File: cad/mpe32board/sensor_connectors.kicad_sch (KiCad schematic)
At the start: 41 parts, among them J10 Conn_01x06, J11 Conn_01x06, J12 Conn_01x06, J13 Conn_01x06, J14 Conn_01x06, J15 Conn_01x06, J16 Conn_01x06, J17 Conn_01x06, J18 Conn_01x06, J19 Conn_01x06, J20 Conn_01x06, J21 Conn_01x06, J22 Conn_01x06, J23 Conn_01x06, J24 Conn_01x06, J25 Conn_01x06, J26 Conn_01x06, J27 Conn_01x06, J28 Conn_01x06, J29 Conn_01x06, J3 Conn_01x04, J30 Conn_01x06, J31 Conn_01x06, J32 Conn_01x06, J33 Conn_01x06, J34 Conn_01x06, J35 Conn_01x06, J36 Conn_01x06, J37 Conn_01x06, J38 Conn_01x06, J39 Conn_01x06, J4 Conn_01x06, J40 Conn_01x06, J41 Conn_01x06, J42 Conn_01x06, J43 Conn_01x06, J5 Conn_01x06, J6 Conn_01x06, J7 Conn_01x06, J8 Conn_01x06, J9 Conn_01x06

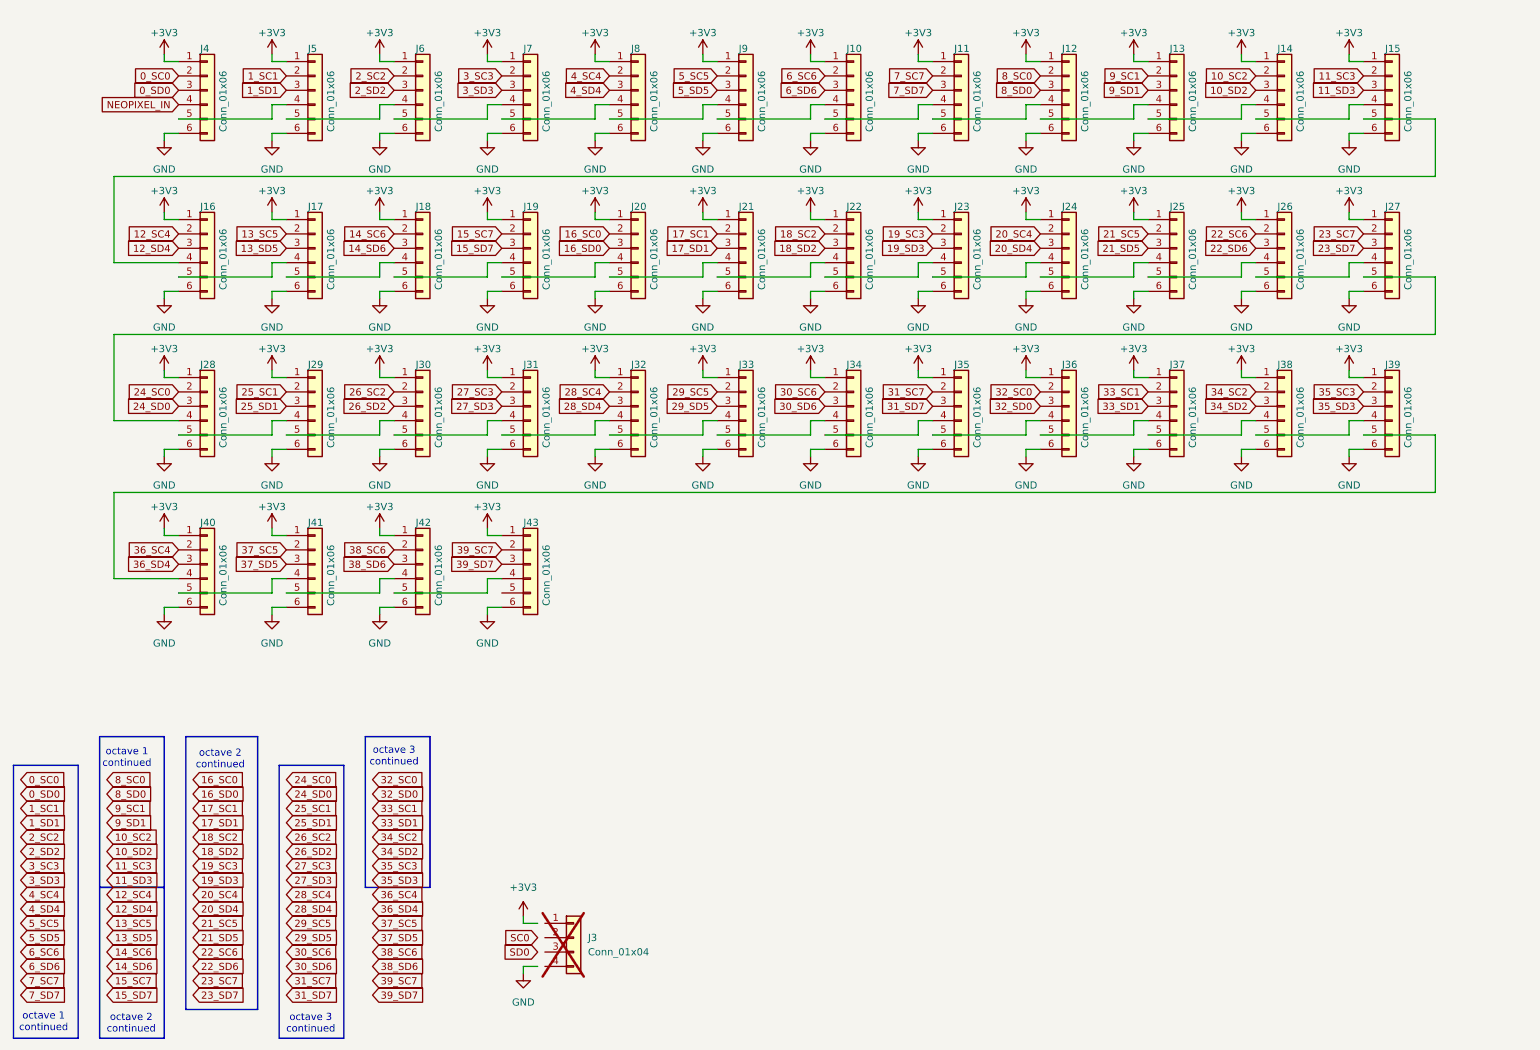
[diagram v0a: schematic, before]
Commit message: add sdram
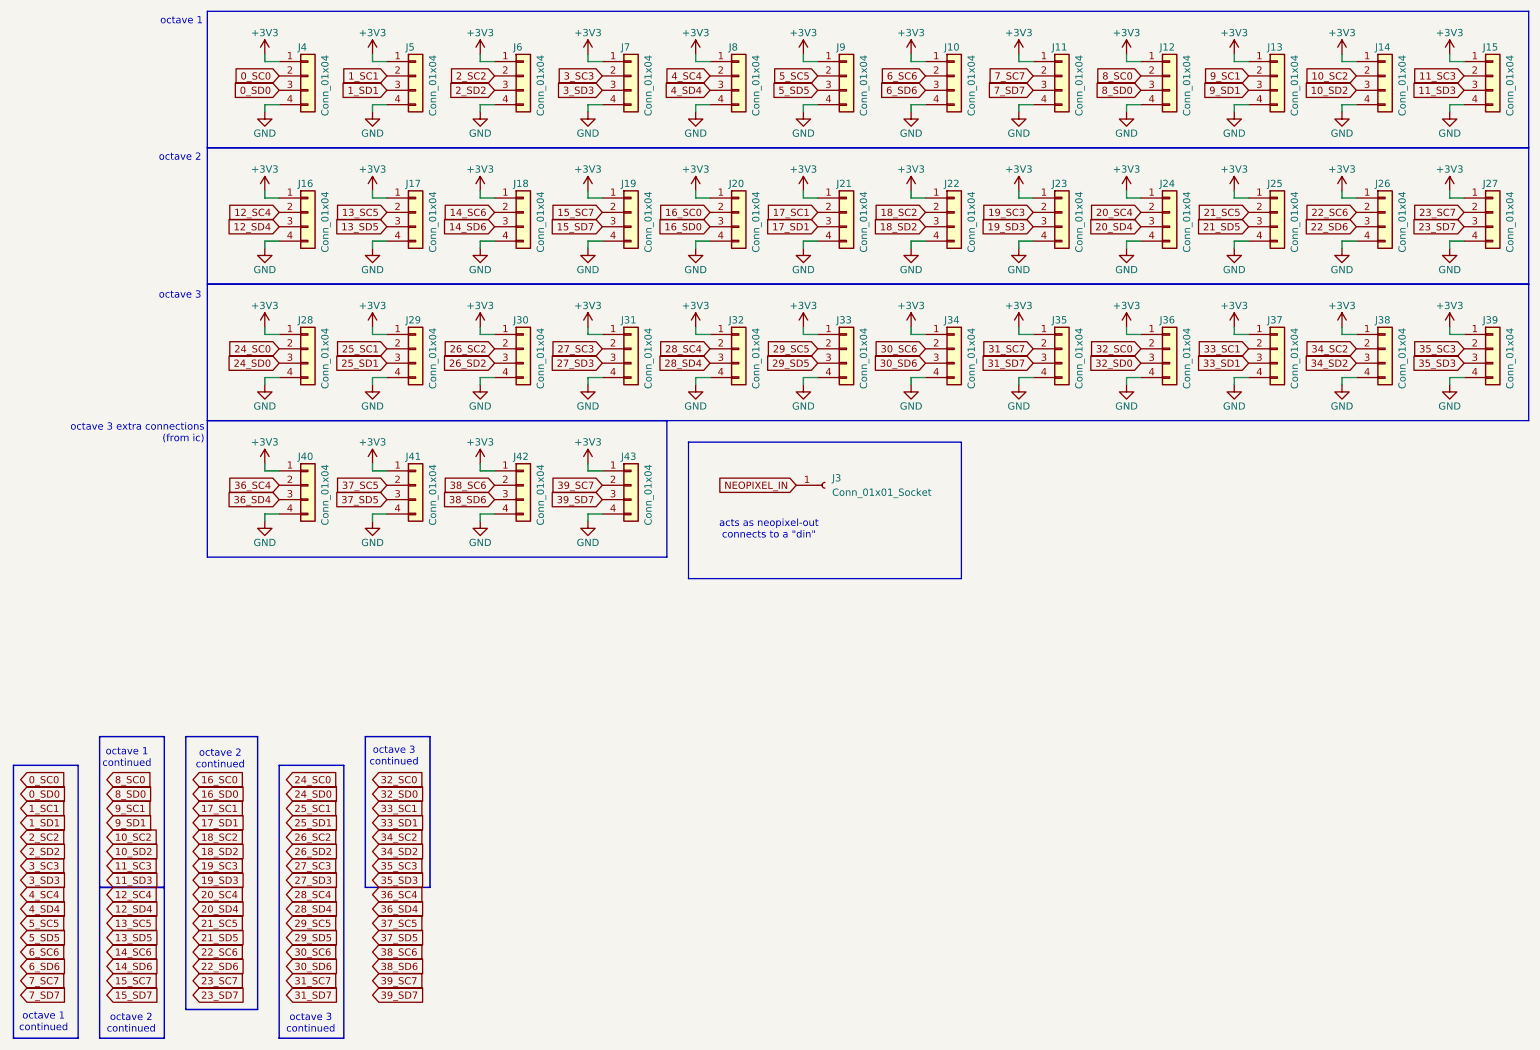
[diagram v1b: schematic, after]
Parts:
- removed J10, J11, J12, J13, J14, J15, J16, J17, J18, J19, J20, J21, J22, J23, J24, J25, J26, J27, J28, J29, J30, J31, J32, J33, J34, J35, J36, J37, J38, J39, J4, J40, J41, J42, J43, J5, J6, J7, J8, J9: Conn_01x06, Connector_JST:JST_SH_BM06B-SRSS-TB_1x06-1MP_P1.00mm_Vertical, symbol Connector_Generic:Conn_01x06
- removed J3: Conn_01x04, Connector_JST:JST_SH_BM04B-SRSS-TB_1x04-1MP_P1.00mm_Vertical, symbol Connector_Generic:Conn_01x04
- added J10, J11, J12, J13, J14, J15, J16, J17, J18, J19, J20, J21, J22, J23, J24, J25, J26, J27, J28, J29, J30, J31, J32, J33, J34, J35, J36, J37, J38, J39, J40, J41, J42, J43, J5, J6, J7, J8, J9: Conn_01x04, symbol Connector_Generic:Conn_01x04
- added J3: Conn_01x01_Socket, Connector_PinSocket_2.54mm:PinSocket_1x01_P2.54mm_Vertical, symbol Connector:Conn_01x01_Socket
- added J4: Conn_01x04, Connector_JST:JST_SH_BM04B-SRSS-TB_1x04-1MP_P1.00mm_Vertical, symbol Connector_Generic:Conn_01x04
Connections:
- net +3V3: now also J10.1 (Pin_1), J11.1 (Pin_1), J12.1 (Pin_1), J13.1 (Pin_1), J14.1 (Pin_1), J15.1 (Pin_1), J16.1 (Pin_1), J17.1 (Pin_1), J18.1 (Pin_1), J19.1 (Pin_1), J20.1 (Pin_1), J21.1 (Pin_1), J22.1 (Pin_1), J23.1 (Pin_1), J24.1 (Pin_1), J25.1 (Pin_1), J26.1 (Pin_1), J27.1 (Pin_1), J28.1 (Pin_1), J29.1 (Pin_1), J30.1 (Pin_1), J31.1 (Pin_1), J32.1 (Pin_1), J33.1 (Pin_1), J34.1 (Pin_1), J35.1 (Pin_1), J36.1 (Pin_1), J37.1 (Pin_1), J38.1 (Pin_1), J39.1 (Pin_1), J4.1 (Pin_1), J40.1 (Pin_1), J41.1 (Pin_1), J42.1 (Pin_1), J43.1 (Pin_1), J5.1 (Pin_1), J6.1 (Pin_1), J7.1 (Pin_1), J8.1 (Pin_1), J9.1 (Pin_1)
- net 0_SC0: now also J4.2 (Pin_2)
- net 0_SD0: now also J4.3 (Pin_3)
- net 10_SC2: now also J14.2 (Pin_2)
- net 10_SD2: now also J14.3 (Pin_3)
- net 11_SC3: now also J15.2 (Pin_2)
- net 11_SD3: now also J15.3 (Pin_3)
- net 12_SC4: now also J16.2 (Pin_2)
- net 12_SD4: now also J16.3 (Pin_3)
- net 13_SC5: now also J17.2 (Pin_2)
- net 13_SD5: now also J17.3 (Pin_3)
- net 14_SC6: now also J18.2 (Pin_2)
- net 14_SD6: now also J18.3 (Pin_3)
- net 15_SC7: now also J19.2 (Pin_2)
- net 15_SD7: now also J19.3 (Pin_3)
- net 16_SC0: now also J20.2 (Pin_2)
- net 16_SD0: now also J20.3 (Pin_3)
- net 17_SC1: now also J21.2 (Pin_2)
- net 17_SD1: now also J21.3 (Pin_3)
- net 18_SC2: now also J22.2 (Pin_2)
- net 18_SD2: now also J22.3 (Pin_3)
- net 19_SC3: now also J23.2 (Pin_2)
- net 19_SD3: now also J23.3 (Pin_3)
- net 1_SC1: now also J5.2 (Pin_2)
- net 1_SD1: now also J5.3 (Pin_3)
- net 20_SC4: now also J24.2 (Pin_2)
- net 20_SD4: now also J24.3 (Pin_3)
- net 21_SC5: now also J25.2 (Pin_2)
- net 21_SD5: now also J25.3 (Pin_3)
- net 22_SC6: now also J26.2 (Pin_2)
- net 22_SD6: now also J26.3 (Pin_3)
- net 23_SC7: now also J27.2 (Pin_2)
- net 23_SD7: now also J27.3 (Pin_3)
- net 24_SC0: now also J28.2 (Pin_2)
- net 24_SD0: now also J28.3 (Pin_3)
- net 25_SC1: now also J29.2 (Pin_2)
- net 25_SD1: now also J29.3 (Pin_3)
- net 26_SC2: now also J30.2 (Pin_2)
- net 26_SD2: now also J30.3 (Pin_3)
- net 27_SC3: now also J31.2 (Pin_2)
- net 27_SD3: now also J31.3 (Pin_3)
- net 28_SC4: now also J32.2 (Pin_2)
- net 28_SD4: now also J32.3 (Pin_3)
- net 29_SC5: now also J33.2 (Pin_2)
- net 29_SD5: now also J33.3 (Pin_3)
- net 2_SC2: now also J6.2 (Pin_2)
- net 2_SD2: now also J6.3 (Pin_3)
- net 30_SC6: now also J34.2 (Pin_2)
- net 30_SD6: now also J34.3 (Pin_3)
- net 31_SC7: now also J35.2 (Pin_2)
- net 31_SD7: now also J35.3 (Pin_3)
- net 32_SC0: now also J36.2 (Pin_2)
- net 32_SD0: now also J36.3 (Pin_3)
- net 33_SC1: now also J37.2 (Pin_2)
- net 33_SD1: now also J37.3 (Pin_3)
- net 34_SC2: now also J38.2 (Pin_2)
- net 34_SD2: now also J38.3 (Pin_3)
- net 35_SC3: now also J39.2 (Pin_2)
- net 35_SD3: now also J39.3 (Pin_3)
- net 36_SC4: now also J40.2 (Pin_2)
- net 36_SD4: now also J40.3 (Pin_3)
- net 37_SC5: now also J41.2 (Pin_2)
- net 37_SD5: now also J41.3 (Pin_3)
- net 38_SC6: now also J42.2 (Pin_2)
- net 38_SD6: now also J42.3 (Pin_3)
- net 39_SC7: now also J43.2 (Pin_2)
- net 39_SD7: now also J43.3 (Pin_3)
- net 3_SC3: now also J7.2 (Pin_2)
- net 3_SD3: now also J7.3 (Pin_3)
- net 4_SC4: now also J8.2 (Pin_2)
- net 4_SD4: now also J8.3 (Pin_3)
- net 5_SC5: now also J9.2 (Pin_2)
- net 5_SD5: now also J9.3 (Pin_3)
- net 6_SC6: now also J10.2 (Pin_2)
- net 6_SD6: now also J10.3 (Pin_3)
- net 7_SC7: now also J11.2 (Pin_2)
- net 7_SD7: now also J11.3 (Pin_3)
- net 8_SC0: now also J12.2 (Pin_2)
- net 8_SD0: now also J12.3 (Pin_3)
- net 9_SC1: now also J13.2 (Pin_2)
- net 9_SD1: now also J13.3 (Pin_3)
- net GND: now also J10.4 (Pin_4), J11.4 (Pin_4), J12.4 (Pin_4), J13.4 (Pin_4), J14.4 (Pin_4), J15.4 (Pin_4), J16.4 (Pin_4), J17.4 (Pin_4), J18.4 (Pin_4), J19.4 (Pin_4), J20.4 (Pin_4), J21.4 (Pin_4), J22.4 (Pin_4), J23.4 (Pin_4), J24.4 (Pin_4), J25.4 (Pin_4), J26.4 (Pin_4), J27.4 (Pin_4), J28.4 (Pin_4), J29.4 (Pin_4), J30.4 (Pin_4), J31.4 (Pin_4), J32.4 (Pin_4), J33.4 (Pin_4), J34.4 (Pin_4), J35.4 (Pin_4), J36.4 (Pin_4), J37.4 (Pin_4), J38.4 (Pin_4), J39.4 (Pin_4), J4.4 (Pin_4), J40.4 (Pin_4), J41.4 (Pin_4), J42.4 (Pin_4), J43.4 (Pin_4), J5.4 (Pin_4), J6.4 (Pin_4), J7.4 (Pin_4), J8.4 (Pin_4), J9.4 (Pin_4)
- net NEOPIXEL_IN: now also J3.1 (Pin_1)
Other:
- note added: "acts as neopixel-out connects to a "din""
- note added: "octave 1"
- note added: "octave 2"
- note added: "octave 3"
- note added: "octave 3 extra connections (from ic)"
